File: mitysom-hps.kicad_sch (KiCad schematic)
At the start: 7 parts, among them J100 Plug_Samtec_SEAM-50-02.0-L-08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

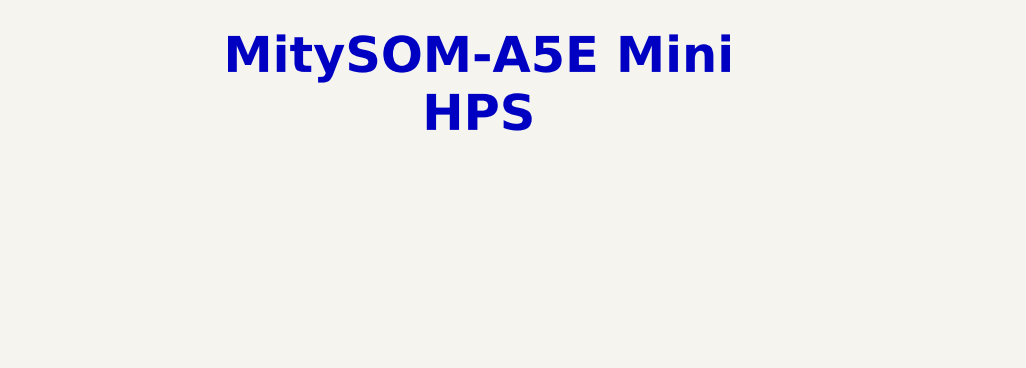
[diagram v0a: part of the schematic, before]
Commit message: [#100282] Add missing schematic sheet names and align them all
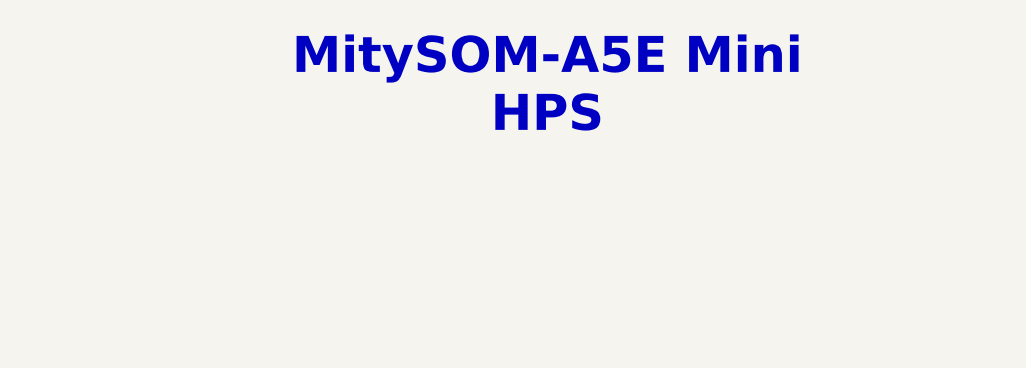
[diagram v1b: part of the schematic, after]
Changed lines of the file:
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@@
 	(text "MitySOM-A5E Mini\nHPS"
 		(exclude_from_sim no)
-		(at 203.2 38.1 0)
+		(at 210.82 38.1 0)
 		(effects
 			(font

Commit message: [#100501] Gate GbE_PHY_RESET with COLD_RESET signal, to reset ETH PHY
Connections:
- net ~{GbE_RESET} renamed ~{GbE_PHY_RESET}
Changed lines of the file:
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@@
 		)
 	)
-	(hierarchical_label "~{GbE_RESET}"
+	(hierarchical_label "~{GbE_PHY_RESET}"
 		(shape output)
 		(at 222.25 171.45 0)

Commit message: [#100501] Reannotate schematic
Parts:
- renumbered J100 to J1, R301 to R3, R302 to R4, R303 to R5, R304 to R6, R305 to R7, R306 to R8
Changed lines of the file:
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@@
 		(in_pos_files yes)
 		(dnp no)
-		(property "Reference" "R301"
+		(property "Reference" "R3"
 			(at 237.49 124.46 0)
 			(show_name no)
@@
 			(project "altera-modular-agilex-5-dc-scm"
 				(path "/6bb9d978-a328-4b30-874b-55170a976185/28ef639c-9de1-4cc9-9bdd-2421ace540ac"
-					(reference "R301")
+					(reference "R3")
 					(unit 1)
 				)
@@
 		(in_pos_files yes)
 		(dnp no)
-		(property "Reference" "R306"
+		(property "Reference" "R8"
 			(at 237.49 147.32 0)
 			(show_name no)
@@
 			(project "altera-modular-agilex-5-dc-scm"
 				(path "/6bb9d978-a328-4b30-874b-55170a976185/28ef639c-9de1-4cc9-9bdd-2421ace540ac"
-					(reference "R306")
+					(reference "R8")
 					(unit 1)
 				)
@@
 		(in_pos_files yes)
 		(dnp no)
-		(property "Reference" "R303"
+		(property "Reference" "R5"
 			(at 237.49 134.62 0)
 			(show_name no)
@@
 			(project "altera-modular-agilex-5-dc-scm"
 				(path "/6bb9d978-a328-4b30-874b-55170a976185/28ef639c-9de1-4cc9-9bdd-2421ace540ac"
-					(reference "R303")
+					(reference "R5")
 					(unit 1)
 				)
@@
 		(in_pos_files yes)
 		(dnp no)
-		(property "Reference" "R302"
+		(property "Reference" "R4"
 			(at 237.49 127 0)
 			(show_name no)
@@
 			(project "altera-modular-agilex-5-dc-scm"
 				(path "/6bb9d978-a328-4b30-874b-55170a976185/28ef639c-9de1-4cc9-9bdd-2421ace540ac"
-					(reference "R302")
+					(reference "R4")
 					(unit 1)
 				)
@@
 		(dnp no)
 		(fields_autoplaced yes)
-		(property "Reference" "J100"
+		(property "Reference" "J1"
 			(at 203.2 118.11 0)
 			(show_name no)
@@
 			(project "altera-modular-agilex-5-dc-scm"
 				(path "/6bb9d978-a328-4b30-874b-55170a976185/28ef639c-9de1-4cc9-9bdd-2421ace540ac"
-					(reference "J100")
+					(reference "J1")
 					(unit 2)
 				)
@@
 		(in_pos_files yes)
 		(dnp no)
-		(property "Reference" "R304"
+		(property "Reference" "R6"
 			(at 237.49 137.16 0)
 			(show_name no)
@@
 			(project "altera-modular-agilex-5-dc-scm"
 				(path "/6bb9d978-a328-4b30-874b-55170a976185/28ef639c-9de1-4cc9-9bdd-2421ace540ac"
-					(reference "R304")
+					(reference "R6")
 					(unit 1)
 				)
@@
 		(in_pos_files yes)
 		(dnp no)
-		(property "Reference" "R305"
+		(property "Reference" "R7"
 			(at 237.49 144.78 0)
 			(show_name no)
@@
 			(project "altera-modular-agilex-5-dc-scm"
 				(path "/6bb9d978-a328-4b30-874b-55170a976185/28ef639c-9de1-4cc9-9bdd-2421ace540ac"
-					(reference "R305")
+					(reference "R7")
 					(unit 1)
 				)

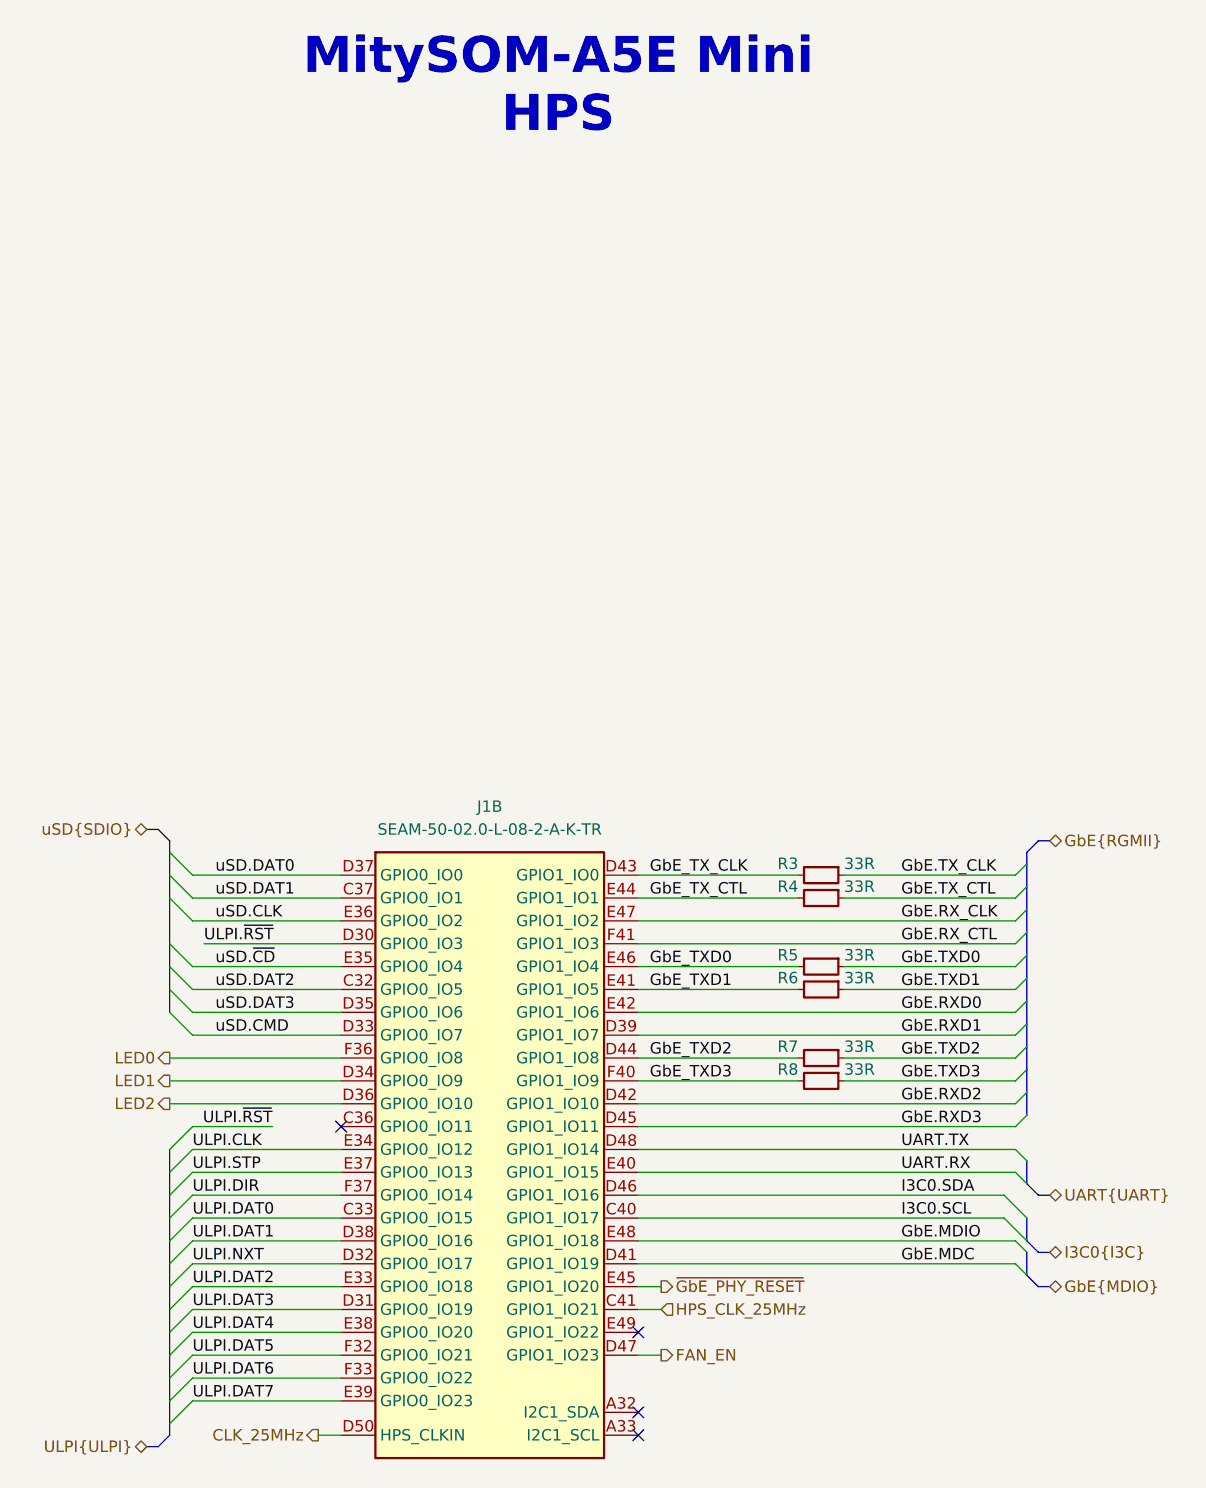
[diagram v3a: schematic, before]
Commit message: [#100595] Update connections according to client request
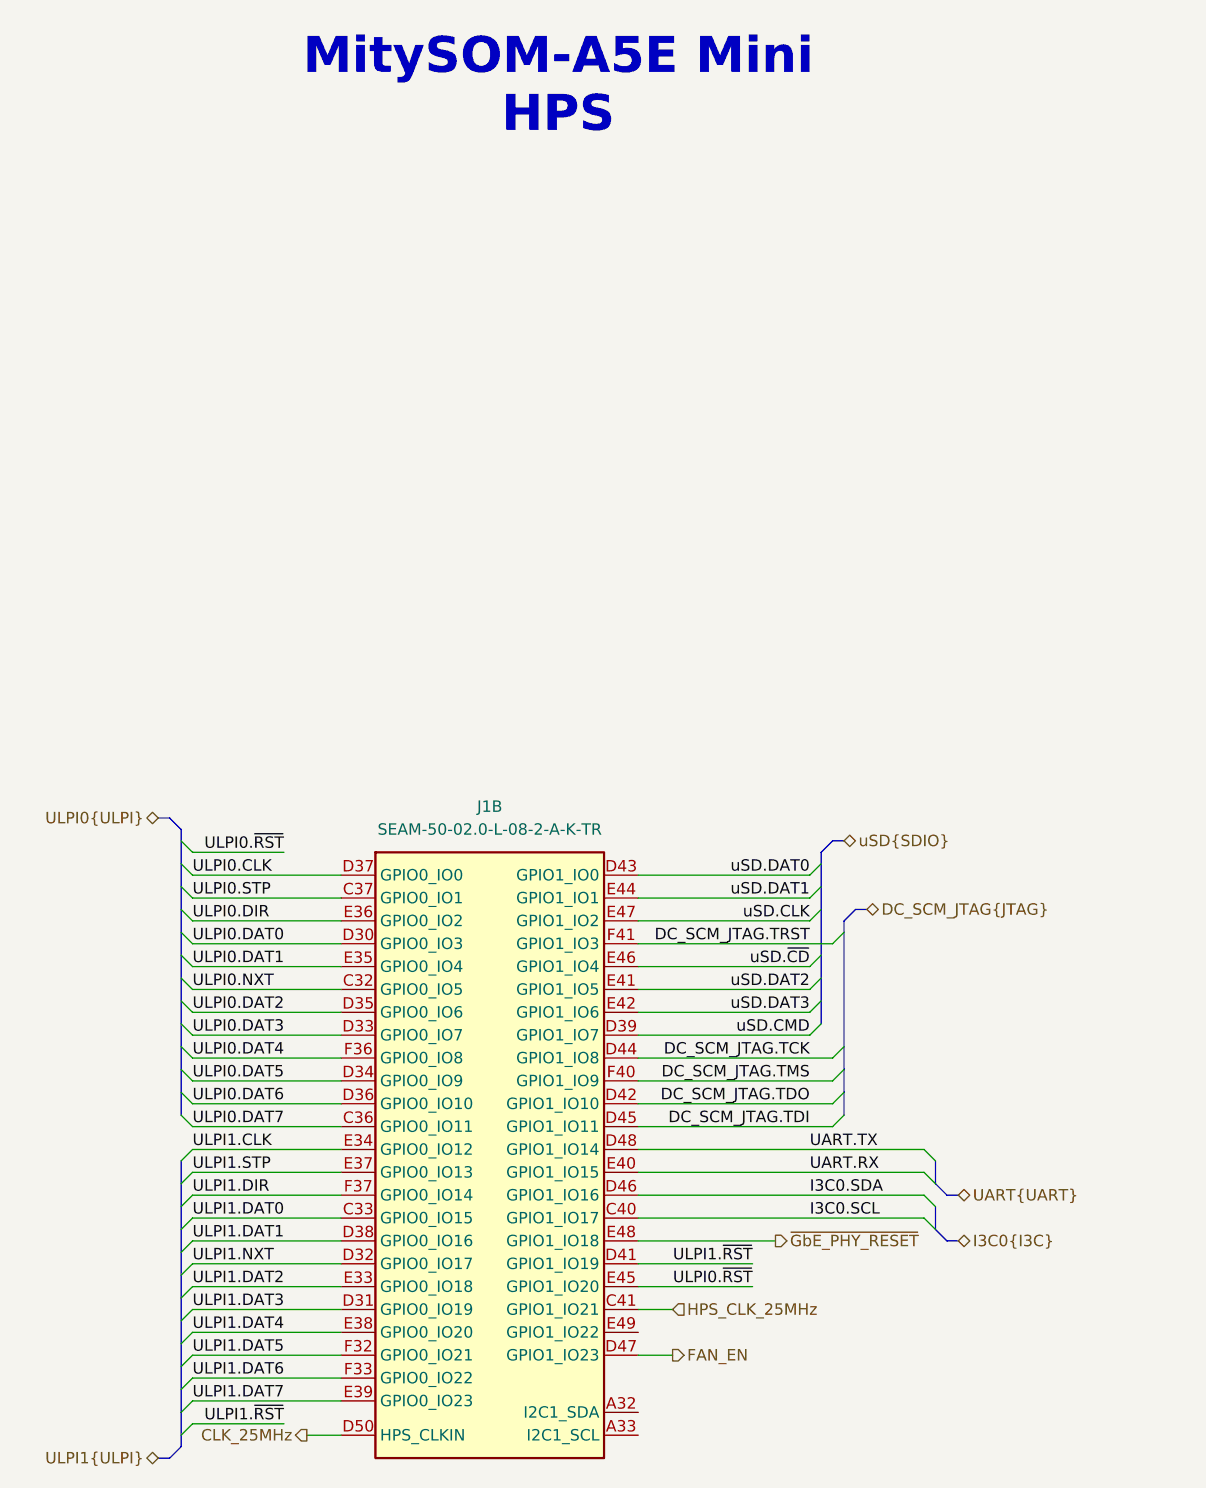
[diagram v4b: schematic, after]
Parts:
- removed R3, R4, R5, R6, R7, R8: R_33R_0402, antmicro-footprints:R_0402_1005Metric, symbol antmicroResistors0402:R_33R_0402
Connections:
- net GbE.MDIO is gone; now on net ~{GbE_PHY_RESET}: J1.E48 (GPIO1_IO18)
- net GbE.RXD0 is gone; now on net uSD.DAT3: J1.E42 (GPIO1_IO6)
- net GbE.RXD1 is gone; now on net uSD.CMD: J1.D39 (GPIO1_IO7)
- net GbE.RX_CLK is gone; now on net uSD.CLK: J1.E47 (GPIO1_IO2)
- net GbE_TXD0 is gone; now on net uSD.~{CD}: J1.E46 (GPIO1_IO4)
- net GbE_TXD1 is gone; now on net uSD.DAT2: J1.E41 (GPIO1_IO5)
- net GbE_TX_CLK is gone; now on net uSD.DAT0: J1.D43 (GPIO1_IO0)
- net GbE_TX_CTL is gone; now on net uSD.DAT1: J1.E44 (GPIO1_IO1)
- net uSD.CLK: no longer J1.E36 (GPIO0_IO2)
- net uSD.CMD: no longer J1.D33 (GPIO0_IO7)
- net uSD.DAT0: no longer J1.D37 (GPIO0_IO0)
- net uSD.DAT1: no longer J1.C37 (GPIO0_IO1)
- net uSD.DAT2: no longer J1.C32 (GPIO0_IO5)
- net uSD.DAT3: no longer J1.D35 (GPIO0_IO6)
- net uSD.~{CD}: no longer J1.E35 (GPIO0_IO4)
- net ~{GbE_PHY_RESET}: no longer J1.E45 (GPIO1_IO20)
- net ULPI0.DAT7: now reaches J1.C36 (GPIO0_IO11)
- net GbE.MDC renamed ULPI1.~{RST}
- net GbE.RXD2 renamed DC_SCM_JTAG.TDO
- net GbE.RXD3 renamed DC_SCM_JTAG.TDI
- net GbE.RX_CTL renamed DC_SCM_JTAG.TRST
- net GbE_TXD2 renamed DC_SCM_JTAG.TCK
- net GbE_TXD3 renamed DC_SCM_JTAG.TMS
- net LED0 renamed ULPI0.DAT4
- net LED1 renamed ULPI0.DAT5
- net LED2 renamed ULPI0.DAT6
- net ULPI.CLK renamed ULPI1.CLK
- net ULPI.DAT0 renamed ULPI1.DAT0
- net ULPI.DAT1 renamed ULPI1.DAT1
- net ULPI.DAT2 renamed ULPI1.DAT2
- net ULPI.DAT3 renamed ULPI1.DAT3
- net ULPI.DAT4 renamed ULPI1.DAT4
- net ULPI.DAT5 renamed ULPI1.DAT5
- net ULPI.DAT6 renamed ULPI1.DAT6
- net ULPI.DAT7 renamed ULPI1.DAT7
- net ULPI.DIR renamed ULPI1.DIR
- net ULPI.NXT renamed ULPI1.NXT
- net ULPI.STP renamed ULPI1.STP
- net ULPI.~{RST} renamed ULPI0.DAT0
- new net ULPI0.CLK: J1.D37 (GPIO0_IO0)
- new net ULPI0.DAT1: J1.E35 (GPIO0_IO4)
- new net ULPI0.DAT2: J1.D35 (GPIO0_IO6)
- new net ULPI0.DAT3: J1.D33 (GPIO0_IO7)
- new net ULPI0.DIR: J1.E36 (GPIO0_IO2)
- new net ULPI0.NXT: J1.C32 (GPIO0_IO5)
- new net ULPI0.STP: J1.C37 (GPIO0_IO1)
- new net ULPI0.~{RST}: J1.E45 (GPIO1_IO20)
- no-connect marks 4 -> 0

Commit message: [#100501] Clean ERC
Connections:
- no-connect marks 0 -> 3
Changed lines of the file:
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@@
 		)
+	)
+	(no_connect
+		(at 219.71 185.42)
+	)
+	(no_connect
+		(at 219.71 187.96)
+	)
+	(no_connect
+		(at 219.71 176.53)
 	)
 	(bus_entry
@@
 			(justify left bottom)
 		)
-		(property "Netclass" "50Ohm-se"
+		(property "Net Class" "50Ohm-se"
 			(at 165.1 125.73 0)
 			(show_name no)
@@
 			(justify left bottom)
 		)
-		(property "Netclass" "50Ohm-se"
+		(property "Net Class" "50Ohm-se"
 			(at 165.1 184.15 0)
 			(show_name no)
